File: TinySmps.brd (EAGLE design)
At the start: 78.5 x 42 mm, 30 parts, among them IC1 LM2596S, IC2 TINY85P, J2 POWER_JACK

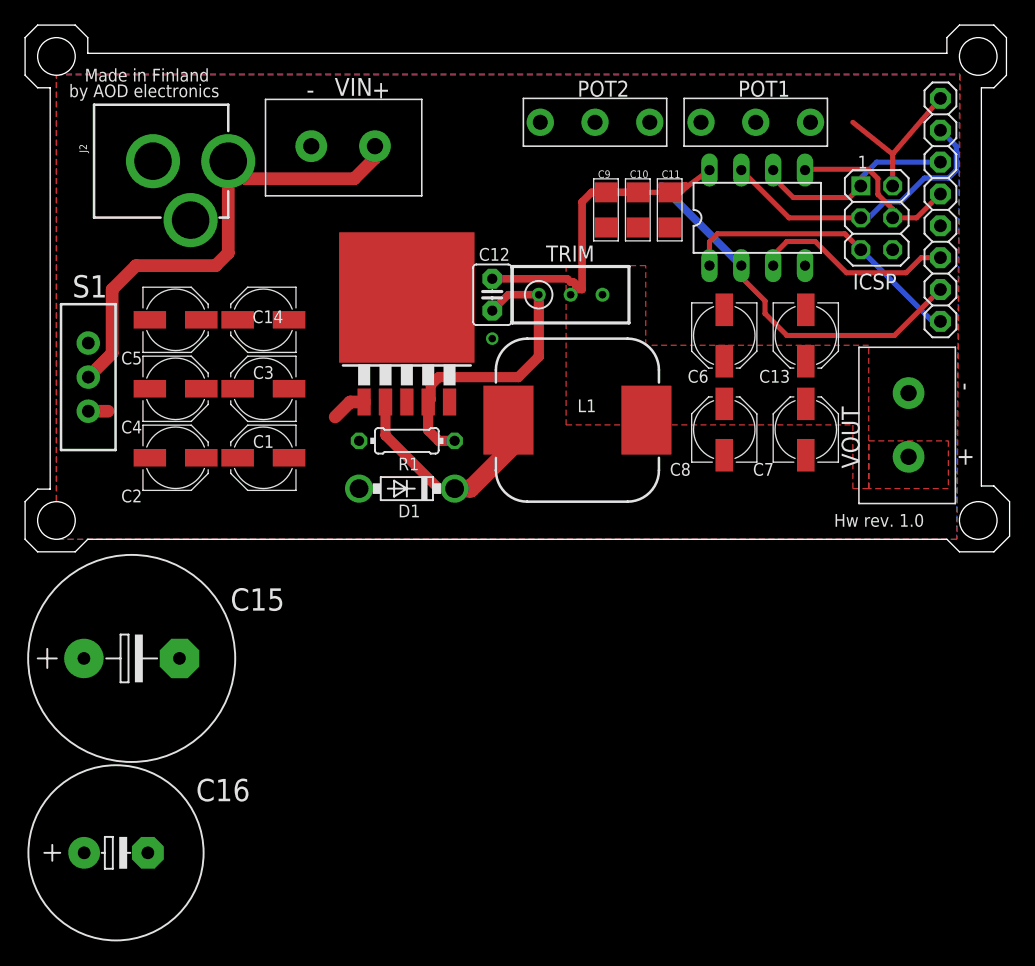
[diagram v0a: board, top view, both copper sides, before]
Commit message: Add files via upload
Changed capacitors, rated for higher input voltage. Added Led status indication for power
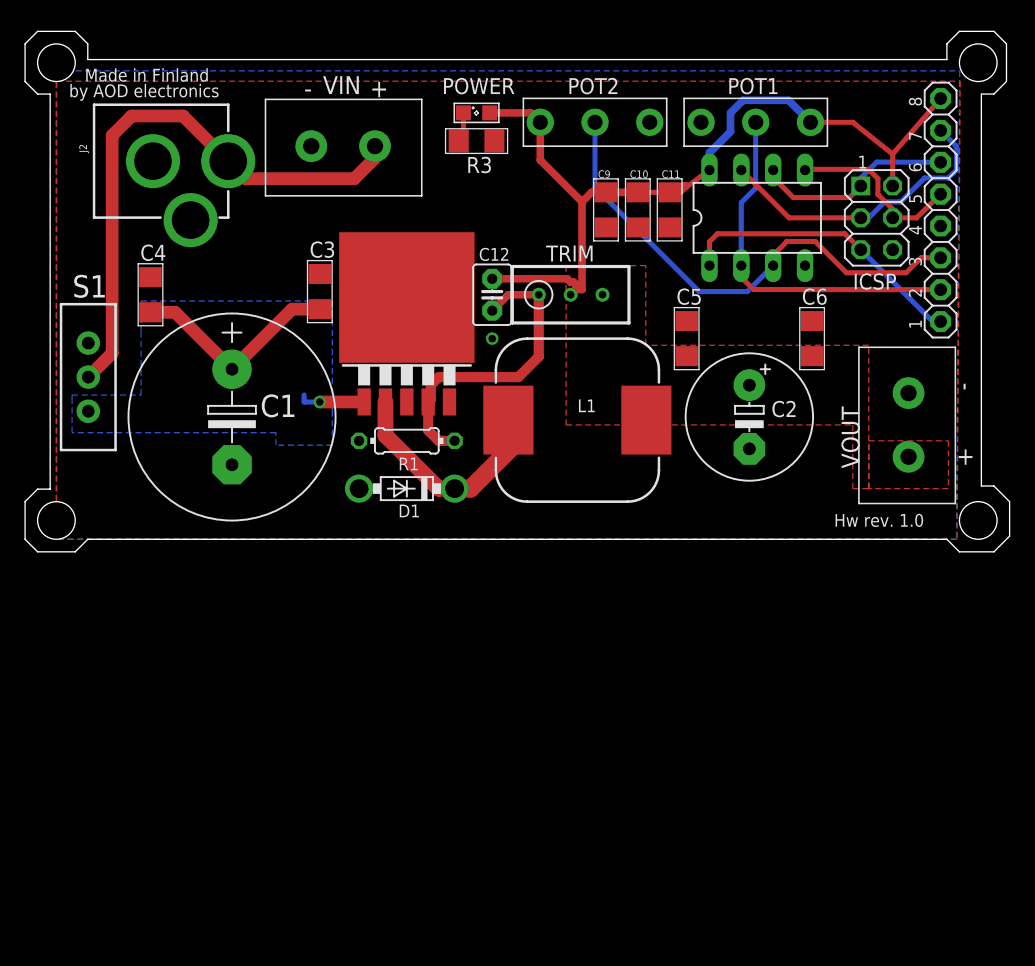
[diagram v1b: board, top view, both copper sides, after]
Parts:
- removed C13, C14, C7, C8: 100u, resistor:PANASONIC_C
- removed C15: (no value), resistor:E7,5-16
- removed C16: (no value), resistor:E5-13
- added POWER: (no value), led:SML0805
- added R3: (no value), resistor:R1206
- C1: value 100u -> (none); device resistor:PANASONIC_C -> resistor:E7,5-16
- C2: value 100u -> (none); device resistor:PANASONIC_C -> resistor:E5-10,5
- C3, C4, C5, C6: value 100u -> (none); device resistor:PANASONIC_C -> rcl:C1206
- moved C2 45.9 mm to (57.8, 10.5), turned to 270 degrees
- moved C5 40.8 mm to (52.8, 16.8), turned to 90 degrees
- moved C3 8.96 mm to (23.5, 20.5), turned to 90 degrees
- moved C4 7.76 mm to (10.0, 20.2), turned to 90 degrees
- moved C6 7.00 mm to (62.8, 16.8), turned to 90 degrees
- moved C1 4.10 mm to (16.5, 10.5), turned to 270 degrees
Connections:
- new net IN: C1.+, C3.1, C4.1, IC1.1, S1.3
- net GND: now also C3.2, C4.2, C5.2, C6.2, R3.1; no longer C13.-, C14.-, C3.-, C4.-, C5.-, C6.-, C7.-, C8.-
- net N$1: now also POWER.C, R3.2; no longer C1.+, C14.+, C2.+, C3.+, C4.+, C5.+, IC1.1, S1.3
- net VCC: now also C2.+, C5.1, C6.1, POWER.A; no longer C13.+, C6.+, C7.+, C8.+
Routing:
- net VCC: track 41.1 -> 69.3 mm
- net PB4: track 16.2 -> 39.9 mm
- net IN: track 0.00 -> 22.7 mm, vias 0 -> 1
- net N$4: track 39.5 -> 45.4 mm
- net N$1: track 4.39 -> 2.40 mm
- net PB3: track 29.8 -> 29.1 mm
- added copper zone on layer 16, net IN
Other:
- board size 78.5 x 42 mm -> 78.5 x 41.5 mm
- board text added: "2"
- board text added: "3"
- board text added: "4"
- board text added: "5"
- board text added: "6"
- board text added: "7"
- board text added: "8"

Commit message: Add files via upload
omar changes
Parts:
- moved C1 0.25 mm to (16.5, 10.8)
- moved C10 0.25 mm to (48.9, 27.3)
- moved C11 0.25 mm to (51.4, 27.3)
- moved C12 0.25 mm to (37.2, 20.5)
- moved C2 0.25 mm to (57.8, 10.8)
- moved C3 0.25 mm to (23.5, 20.8)
- moved C4 0.25 mm to (10.0, 20.5)
- moved C5 0.25 mm to (52.8, 17.0)
- moved C6 0.25 mm to (62.8, 17.0)
- moved C9 0.25 mm to (46.3, 27.3)
- moved D1 0.25 mm to (30.4, 5.04)
- moved IC1 0.25 mm to (30.4, 17.7)
- moved IC2 0.25 mm to (58.4, 26.6)
- moved ICSP 0.25 mm to (67.9, 26.6)
- moved J2 0.25 mm to (2.50, 31.1)
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
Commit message: Add files via upload
Changed some bad routes
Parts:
- moved C3 0.25 mm to (23.5, 20.5)
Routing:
- net N$2: track 19.1 -> 22.1 mm
- net VCC: track 69.1 -> 71.0 mm
- net N$4: track 45.4 -> 46.2 mm
